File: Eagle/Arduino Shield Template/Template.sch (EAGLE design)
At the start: 23 parts, among them M1 ARDUINO_R3_ICSP, X1 SMA, X2 SMA

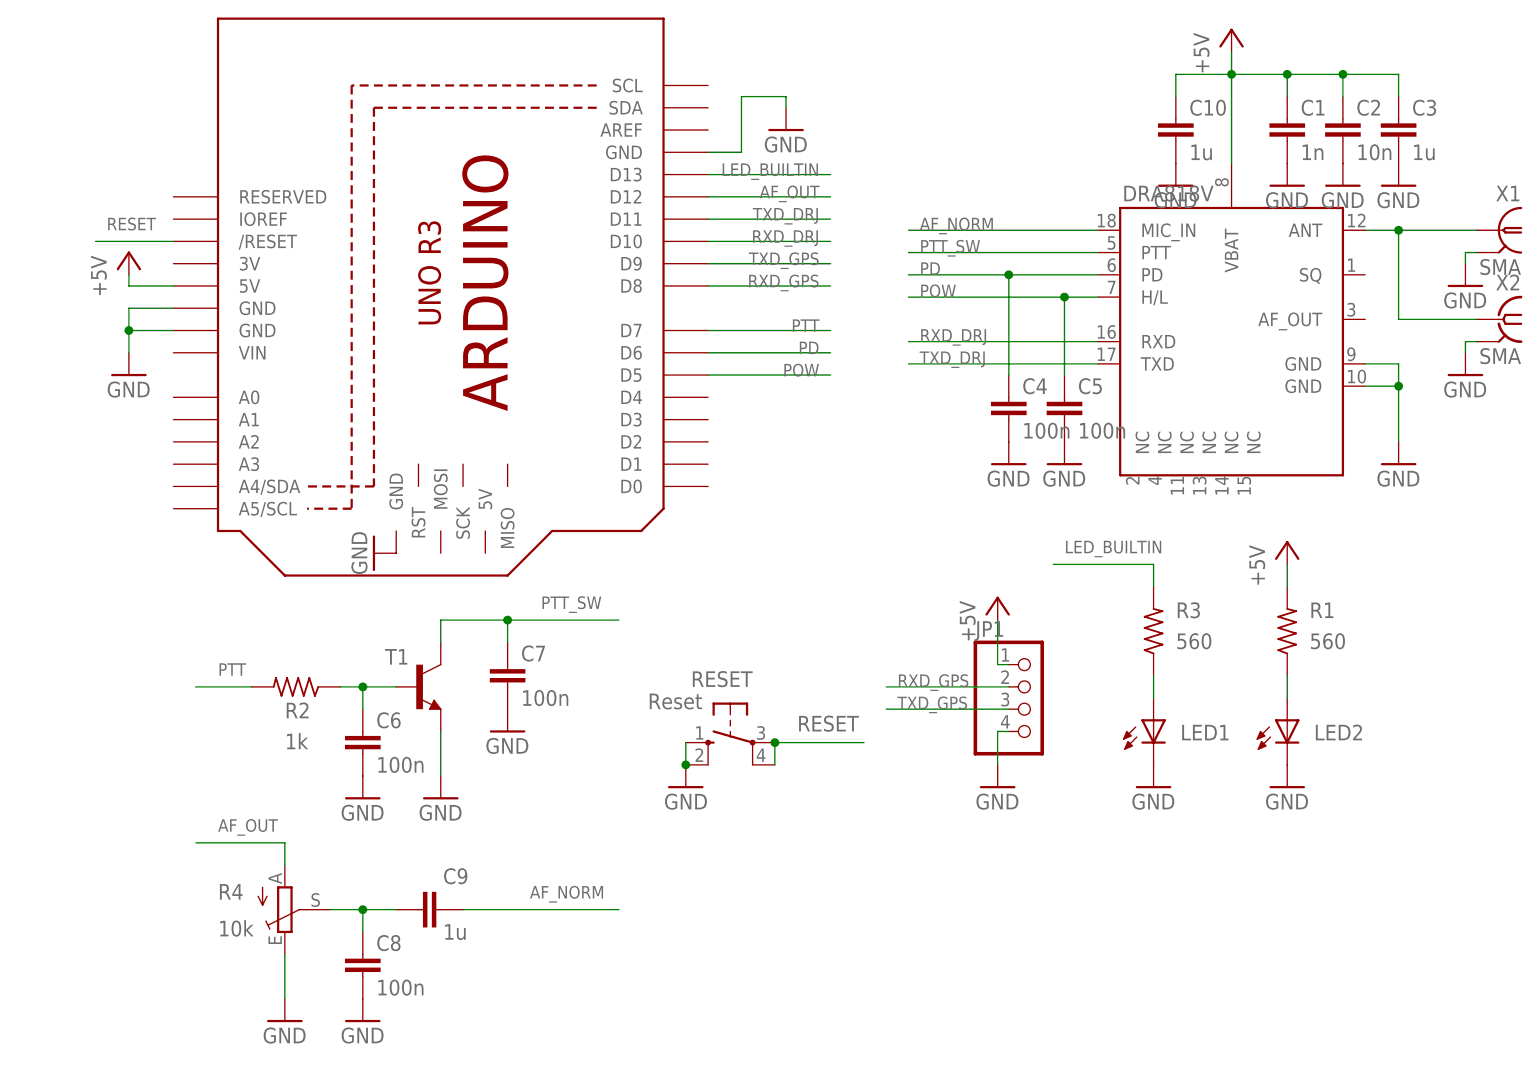
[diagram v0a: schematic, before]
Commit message: Adding Eagle SCH Template
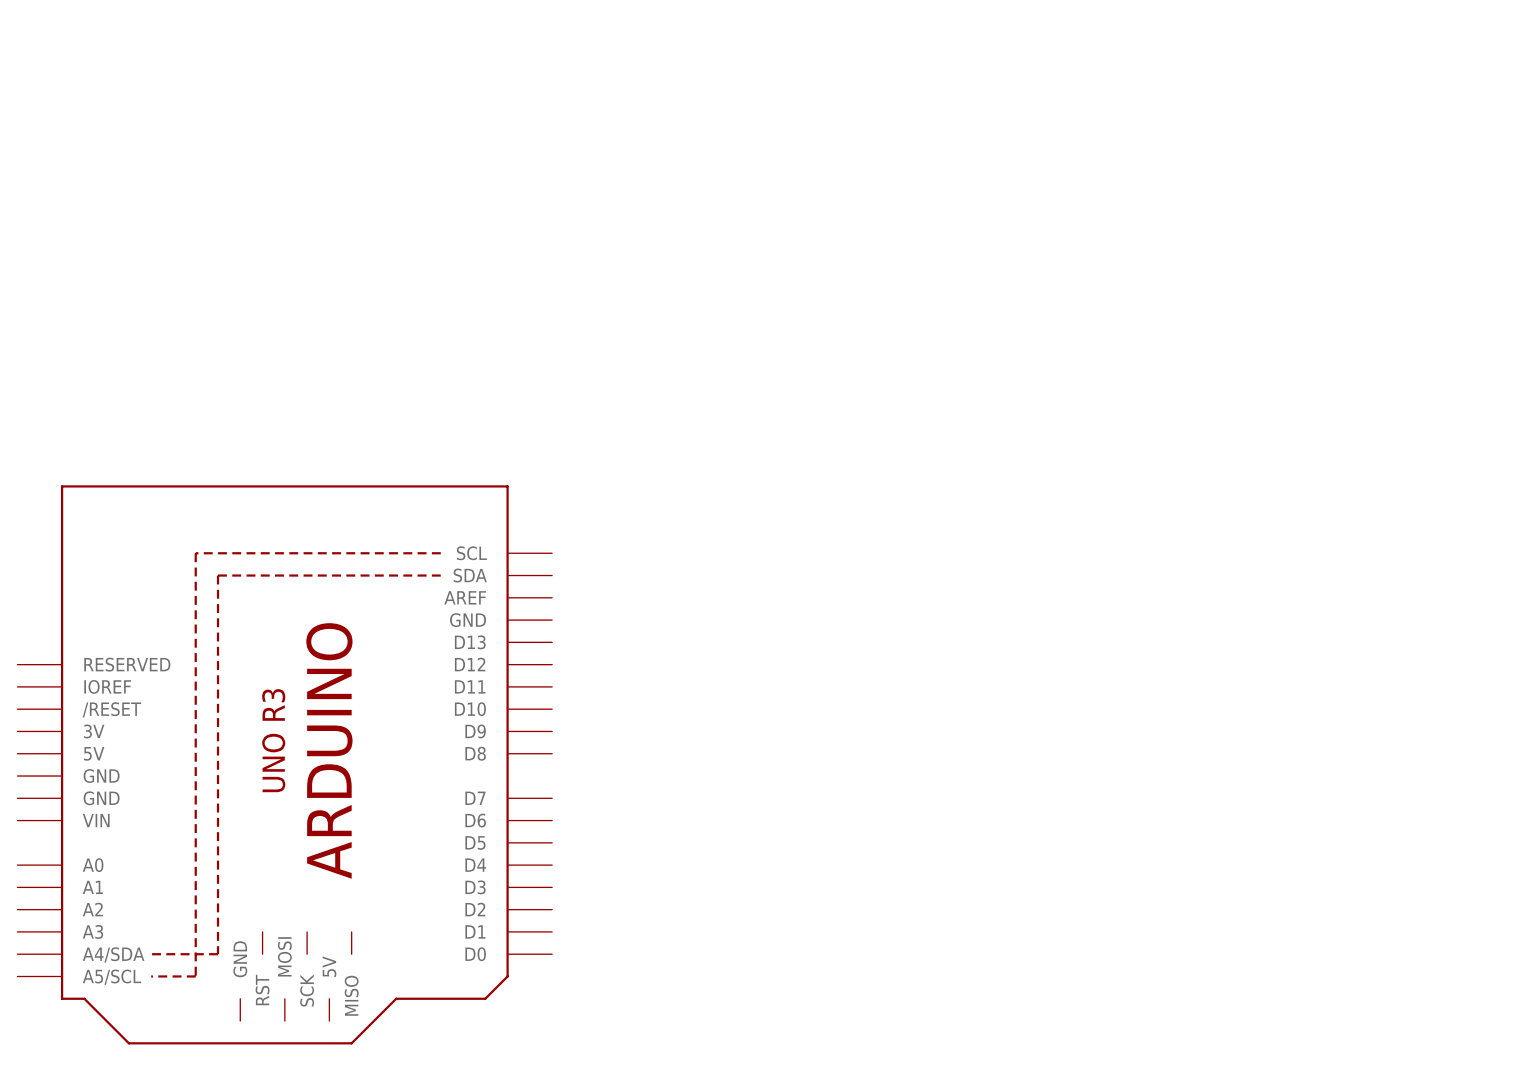
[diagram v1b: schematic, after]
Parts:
- removed C1: 1n, resistor:C-EUC1206
- removed C10, C3, C9: 1u, resistor:C-EUC1206
- removed C2: 10n, resistor:C-EUC1206
- removed C4, C5, C6, C7, C8: 100n, resistor:C-EUC1206
- removed DRA818V: (no value), dorji:DRA818A
- removed JP1: (no value), pinhead:PINHD-1X4
- removed LED1, LED2: (no value), adafruit:LED3MM
- removed R1, R3: 560, resistor:R-US_R1206
- removed R2: 1k, resistor:R-US_R1206
- removed R4: 10k, pot:TRIM_EU-CA6V
- removed RESET: Reset, switch-omron:10-XX
- removed T1: (no value), transistor:MMBT3904LT1-NPN-SOT23-BEC
- removed X1: SMA, con-coax:LTI-SASF54GT
- removed X2: SMA, con-coax:SMA-142-0701-801/806
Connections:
- removed net +5V: C1.1, C10.1, C2.1, C3.1, DRA818V.VBAT, JP1.1, M1.5V, R1.2
- removed net AF_NORM: C9.2, DRA818V.MIC_IN
- removed net AF_OUT: M1.D12, R4.A
- removed net GND: C1.2, C10.2, C2.2, C3.2, C4.2, C5.2, C6.2, C7.2, C8.2, DRA818V.GND@1, DRA818V.GND@2, JP1.4, LED1.C, LED2.C, M1.GND, M1.GND@1, M1.GND@2, M1.GND@3, R4.E, RESET.S, RESET.S1, T1.E, X1.2, X2.2
- removed net LED_BUILTIN: M1.D13, R3.2
- removed net N$41: LED2.A, R1.1
- removed net N$5: DRA818V.ANT, X1.1, X2.1
- removed net N$7: C6.1, R2.1, T1.B
- removed net N$8: LED1.A, R3.1
- removed net N$9: C8.1, C9.1, R4.S
- removed net PD: C4.1, DRA818V.PD, M1.D6
- removed net POW: C5.1, DRA818V.H/L, M1.D5
- removed net PTT: M1.D7, R2.2
- removed net PTT_SW: C7.1, DRA818V.PTT, T1.C
- removed net RESET: M1./RESET, RESET.P, RESET.P1
- removed net RXD_DRJ: DRA818V.RXD, M1.D10
- removed net RXD_GPS: JP1.2, M1.D8
- removed net TXD_DRJ: DRA818V.TXD, M1.D11
- removed net TXD_GPS: JP1.3, M1.D9
